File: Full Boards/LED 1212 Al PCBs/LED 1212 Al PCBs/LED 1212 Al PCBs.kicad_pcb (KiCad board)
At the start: 2 copper layers, 25 x 26.5 mm, 3 parts

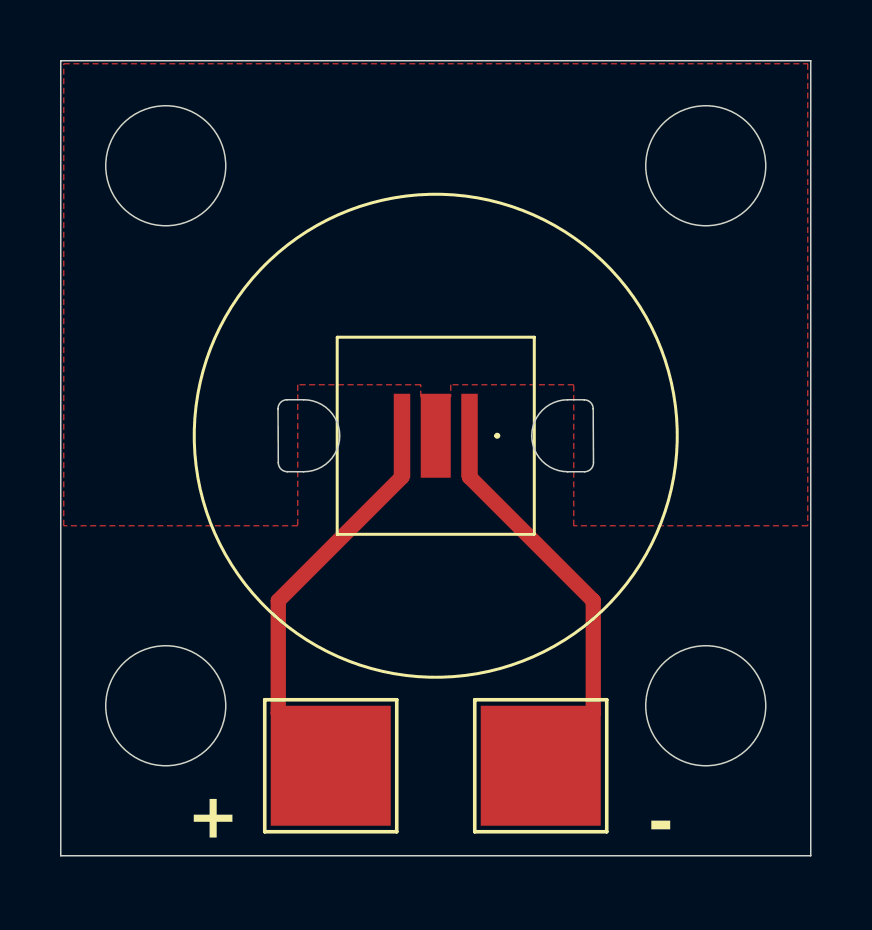
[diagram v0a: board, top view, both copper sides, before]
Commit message: Updated LED 1212 PCB to add solder pads and wire solder pads (replacing what the test points were used for before).
Moved all .stp and .step files back one directory.

Signed-off-by: digimer <digital.mermaid@gmail.com>
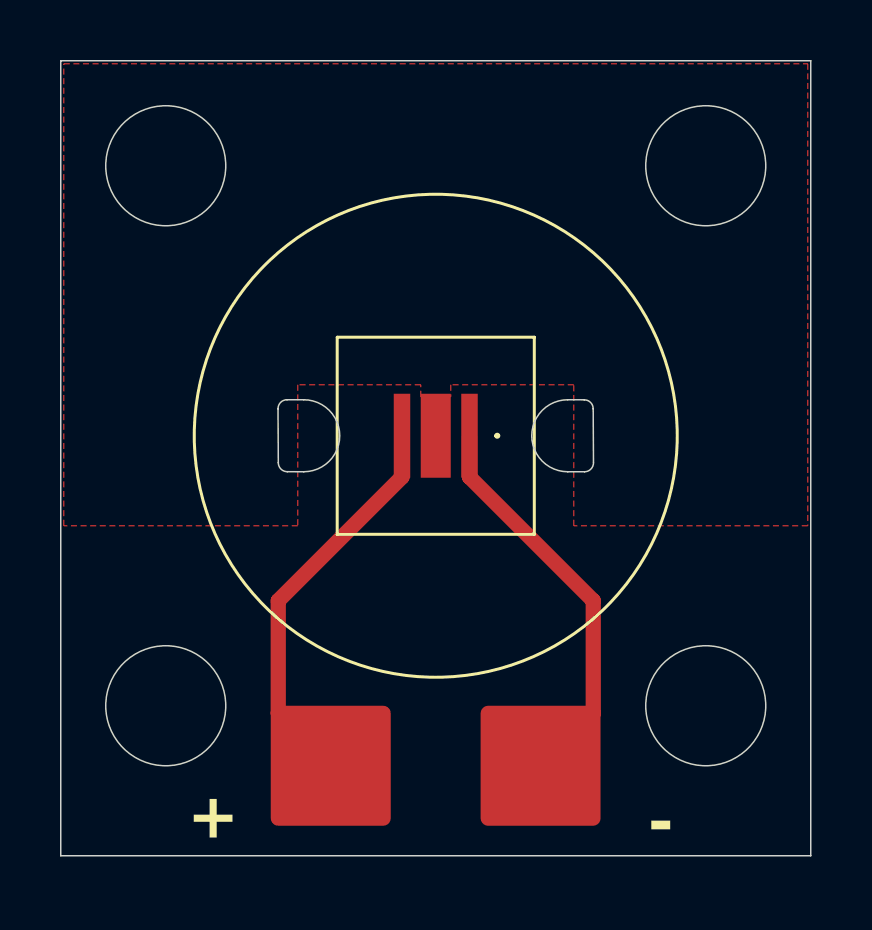
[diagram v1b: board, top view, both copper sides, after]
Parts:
- removed TP1, TP2: TestPoint, TestPoint:TestPoint_Pad_4.0x4.0mm
- added SMD1: - Pad, mr-stuff:SolderWirePad_1x01_SMD_4x4mm, F.Cu at (103.5, 111.0)
- added SMD2: + Pad, mr-stuff:SolderWirePad_1x01_SMD_4x4mm, F.Cu at (96.5, 111.0)
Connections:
- LED1 pad 2: +2.15V -> +2V
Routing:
- net +2.15V: track 13.4 -> 0.00 mm
- net +2V: track 0.00 -> 13.4 mm
